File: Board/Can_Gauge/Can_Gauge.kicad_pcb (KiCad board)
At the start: 2 copper layers, 46 x 46 mm, 33 parts, among them J1 FTDI-Port, J2 CAN, J3 LED 12V, J4 12V, J5 GND, M1 Stepper_Motor, U1 ATMEGA328P-AU, U2 MCP2515-xST, U3 MCP2551-I-SN, U4 L78L05_SOT89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

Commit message: Board adjustments
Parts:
- moved J1 0.94 mm to (162.7, 115.6)
- moved C3 0.92 mm to (161.8, 113.0), turned to 115.4 degrees
- moved R2 0.51 mm to (162.8, 111.2), turned to 115.4 degrees
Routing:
- net TX: track 8.09 -> 7.00 mm
- net RX: track 6.12 -> 5.35 mm
- net Net-(U1-PC6): track 5.08 -> 4.55 mm
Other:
- board size 46 x 46 mm -> 46.1 x 46.1 mm
- board text added: "12V"
- board text added: "12V LED"
- board text added: "CAN H L"
- board text added: "DTR RX TX 5V CTS G"
- board text added: "GND"
- board text added: "JoeM Can Gauge V0.2"
- board text removed: "DTR RX TX 5V CTX G"
- board text removed: "JoeM Can Gauge V0.1"

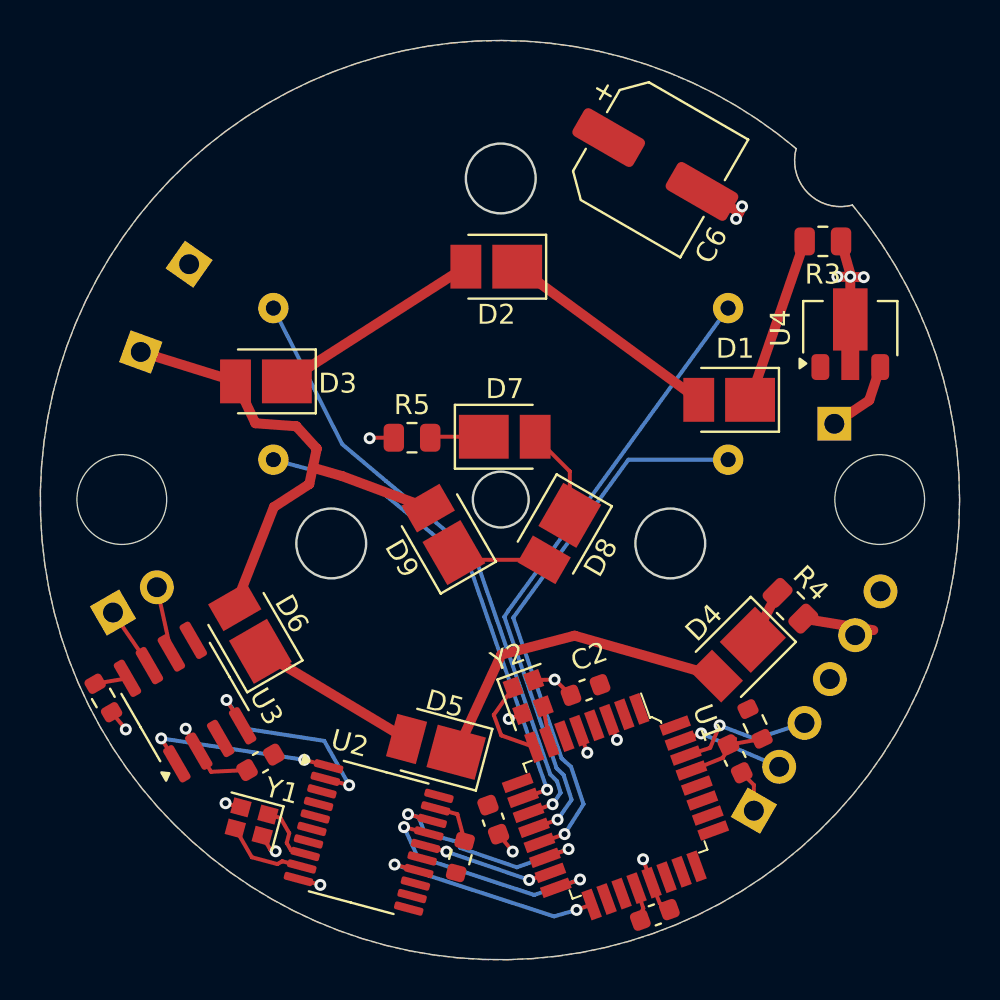
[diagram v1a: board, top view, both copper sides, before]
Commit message: Gauge faces; Init move; restructure Board
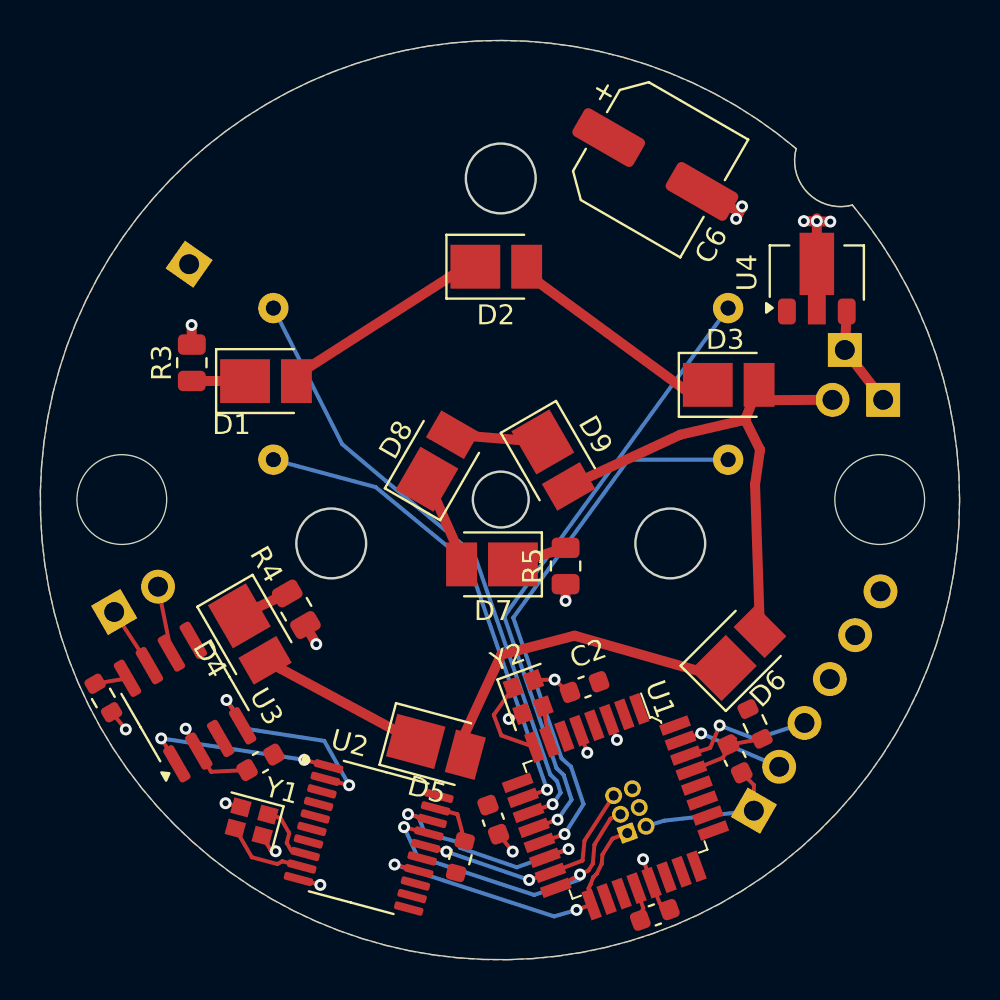
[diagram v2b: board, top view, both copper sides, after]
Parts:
- removed J3: LED 12V, Connector_PinHeader_2.54mm:PinHeader_1x01_P2.54mm_Vertical
- added J6: 12V_LED_Bridge, Connector_PinHeader_2.54mm:PinHeader_1x02_P2.54mm_Vertical, B.Cu at (169.2, 95.0)
- added J7: SPI-Port, Connector_PinHeader_1.00mm:PinHeader_2x03_P1.00mm_Vertical, B.Cu at (156.3, 116.7)
- moved R3 32.2 mm to (134.5, 93.1), turned to -90 degrees
- moved R4 24.8 mm to (139.8, 105.5), turned to 120 degrees
- moved D6 24.5 mm to (161.9, 107.7), turned to 45 degrees
- moved D4 24.5 mm to (137.4, 106.7), turned to -60 degrees
- moved D1 23.2 mm to (138.2, 94.1), turned to 0 degrees
- moved D3 23.2 mm to (161.4, 94.2), turned to 0 degrees
- moved R5 10.0 mm to (153.2, 103.3), turned to 90 degrees
- moved D8 7.11 mm to (146.8, 98.1), turned to 60 degrees
- moved D9 6.65 mm to (152.6, 98.0), turned to -60 degrees
- moved D7 6.43 mm to (149.6, 103.2), turned to 180 degrees
- moved J4 3.74 mm to (167.2, 92.5)
- moved U4 3.25 mm to (165.8, 88.6)
- moved C2 0.16 mm to (154.2, 109.4)
- moved J2 0.07 mm to (130.6, 105.6)
- turned D2 to 0 degrees
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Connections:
- net Net-(U1-PB3) renamed SPI_MISO
- net Net-(U1-PB4) renamed SPI_MOSI
- net Net-(U1-PB5) renamed SPI_CLK
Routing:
- net Net-(D5-A): track 8.54 -> 16.6 mm
- net Net-(D4-A): track 16.6 -> 8.58 mm
- net Net-(D1-K): track 8.40 -> 2.67 mm
- net DTR: track 2.23 -> 7.70 mm
- net SPI_MISO: track 6.60 -> 12.0 mm
- net SPI_CLK: track 11.6 -> 16.1 mm
- net SPI_MOSI: track 12.8 -> 16.8 mm
- net GND: track 32.8 -> 29.2 mm, vias 17 -> 19
- net +12V: track 3.86 -> 5.09 mm
- net 12V_LED: track 26.3 -> 25.2 mm
- net Net-(D2-A): track 10.7 -> 11.3 mm
- net Net-(D1-A): track 11.3 -> 10.7 mm
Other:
- board text removed: "12V"
- board text removed: "12V LED"
- board text removed: "GND"

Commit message: Board: Add protection Diode
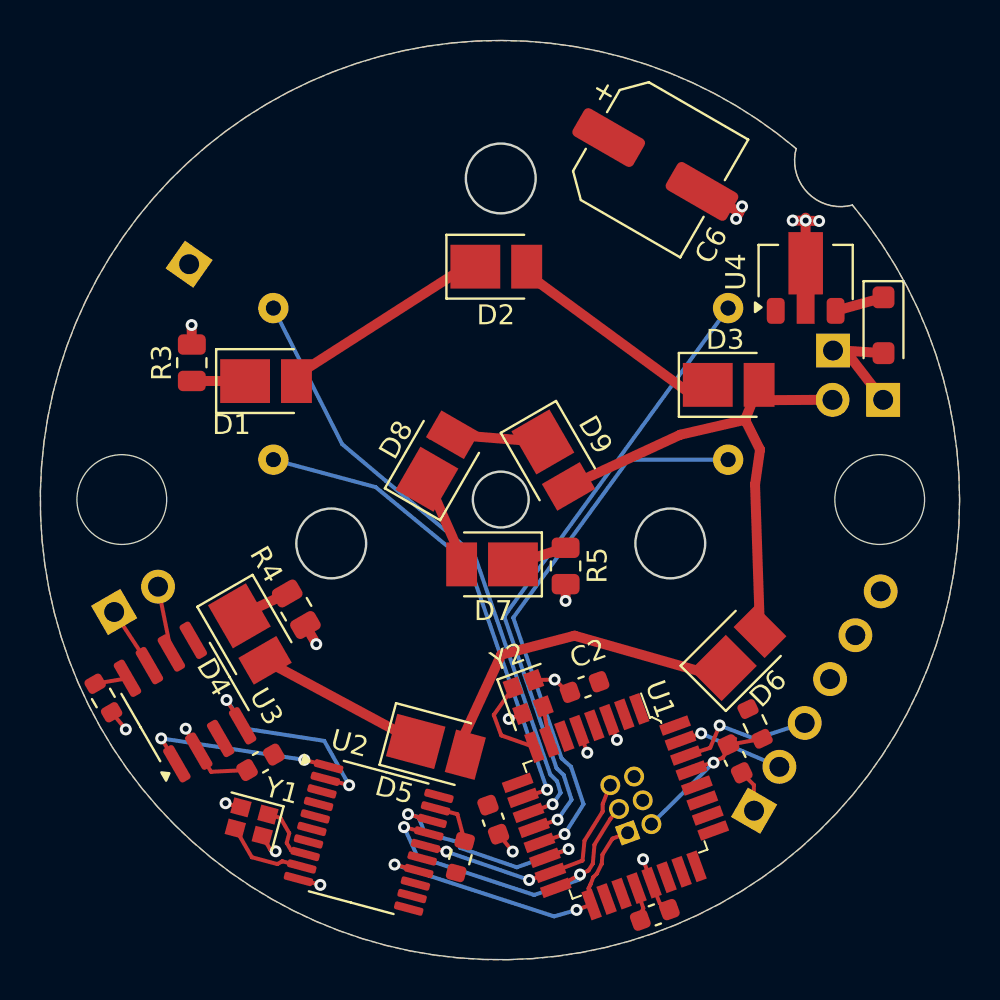
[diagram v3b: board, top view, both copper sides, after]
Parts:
- added D10: D, Diode_SMD:D_SOD-123F, F.Cu at (169.2, 91.3)
- J7: footprint Connector_PinHeader_1.00mm:PinHeader_2x03_P1.00mm_Vertical -> Connector_PinHeader_1.27mm:PinHeader_2x03_P1.27mm_Vertical
- moved J4 0.59 mm to (166.7, 92.5)
- moved U4 0.56 mm to (165.3, 88.6)
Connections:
- C3 pad 2: Net-(U1-PC6) -> Reset
- J7 pad 2: DTR -> Reset
- R2 pad 1: Net-(U1-PC6) -> Reset
- U1 pad 29: Net-(U1-PC6) -> Reset
- U4 pad 3: +12V -> Net-(D10-K)
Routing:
- net Reset: track 0.00 -> 8.94 mm, vias 0 -> 1
- net DTR: track 7.70 -> 2.15 mm
- net Net-(U1-PC6): track 4.55 -> 0.00 mm
- net Net-(D10-K): track 0.00 -> 2.53 mm
- net +12V: track 5.09 -> 5.65 mm
